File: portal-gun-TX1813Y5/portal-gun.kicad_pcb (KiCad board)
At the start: 2 copper layers, 107.2 x 55.5 mm, 10 parts, among them J1 SAO, SW1 SW_Push

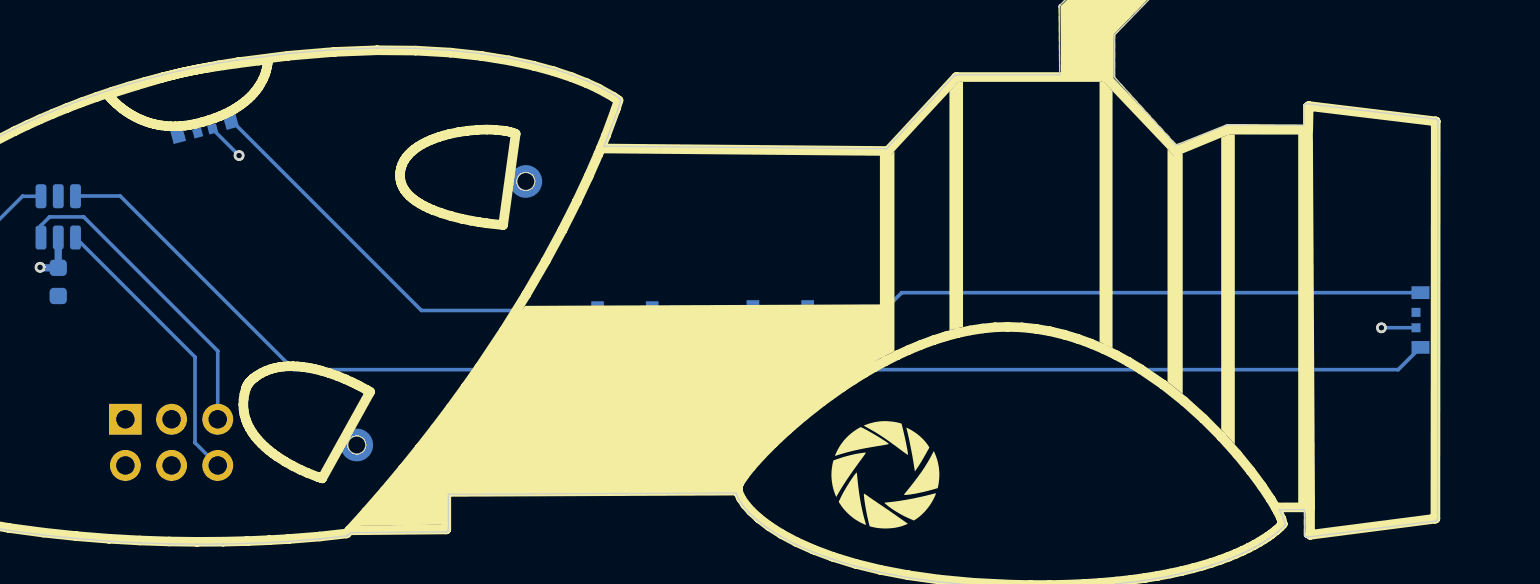
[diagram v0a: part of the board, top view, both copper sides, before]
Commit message: change over to different LED and fix design
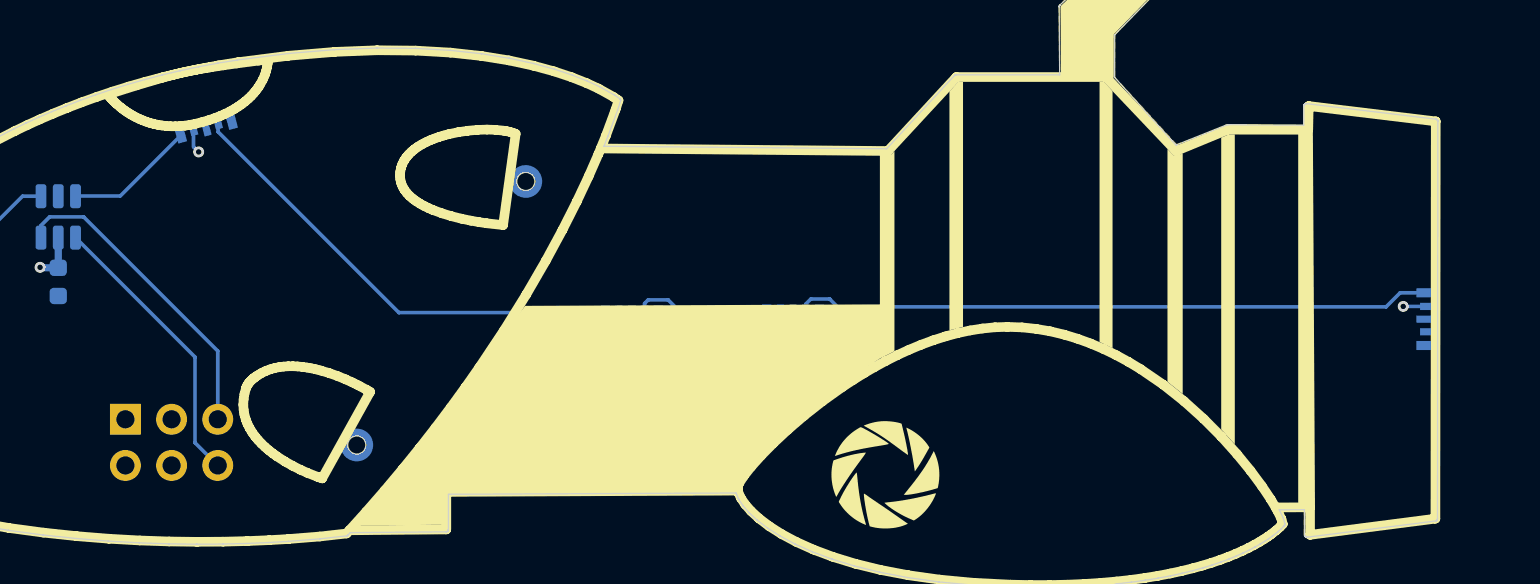
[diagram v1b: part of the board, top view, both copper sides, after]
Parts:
- removed LED1, LED2, LED3, LED4: ~, LED_SMD:LED-SMD_4P_SK6812D-EC3210R
- added U2: ~, LED_SMD:LED-SMD_5P-L3.2-W1.4_TX1813Y5, B.Cu at (128.6, 71.2)
- added U3: ~, LED_SMD:LED-SMD_5P-L3.2-W1.4_TX1813Y5, B.Cu at (152.1, 81.3)
- added U4: ~, LED_SMD:LED-SMD_5P-L3.2-W1.4_TX1813Y5, B.Cu at (160.9, 81.3)
- added U5: ~, LED_SMD:LED-SMD_5P-L3.2-W1.4_TX1813Y5, B.Cu at (195.7, 81.8)
- J1: footprint Connector_PinSocket_2.54mm:IDC-TH_6P-P2.54_DS1013-06SSIB1-B-0 -> Connector_PinHeader_2.54mm:PinHeader_2x03_P2.54mm_Vertical
- moved J1 2.84 mm to (124.2, 87.3), turned to -90 degrees
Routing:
- net Net-(U1-PA5): track 78.5 -> 7.18 mm
- net Net-(U4-DO): track 0.00 -> 34.9 mm
- net Net-(LED1-DOUT): track 34.5 -> 0.00 mm
- net Net-(U2-DO): track 0.00 -> 25.9 mm
- net Net-(LED3-DOUT): track 24.6 -> 0.00 mm
- net Net-(U3-DO): track 0.00 -> 7.48 mm
- net Net-(LED2-DOUT): track 5.57 -> 0.00 mm
